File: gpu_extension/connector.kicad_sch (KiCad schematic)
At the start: 1 part

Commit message: schematic for gpu extension
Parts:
- J501: renamed from J; footprint (none) -> Connector_PinHeader_2.54mm:PinHeader_2x08_P2.54mm_Horizontal

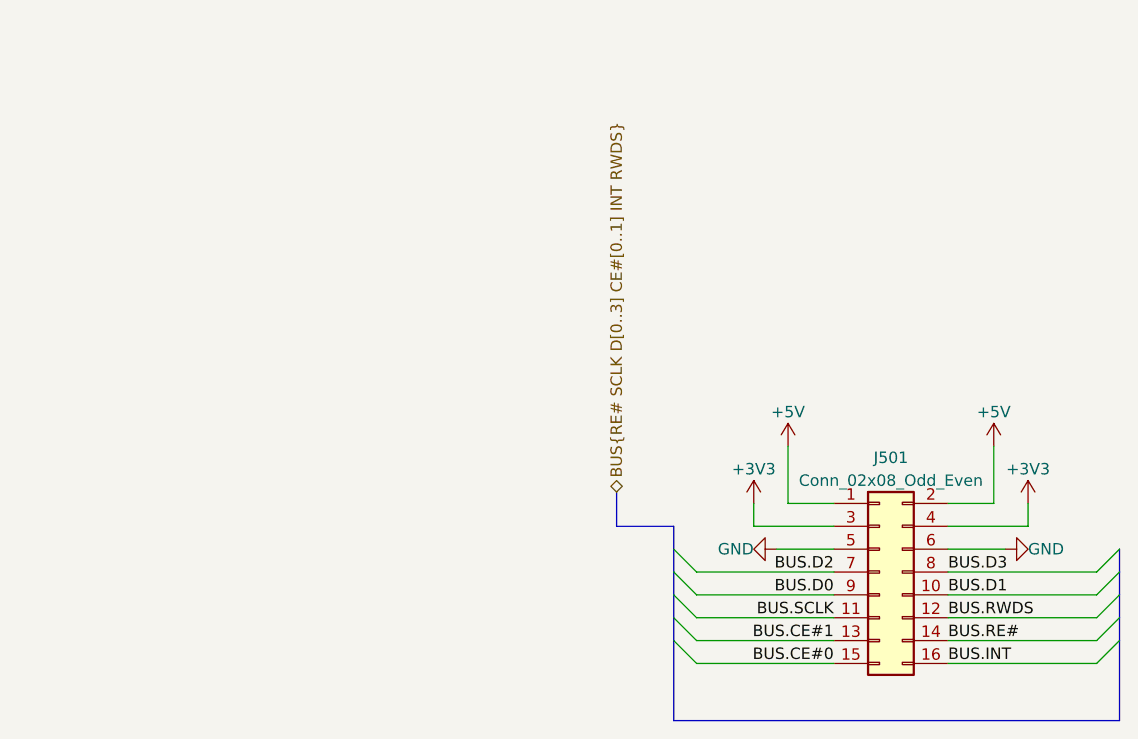
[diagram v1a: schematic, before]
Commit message: some ERC fixes
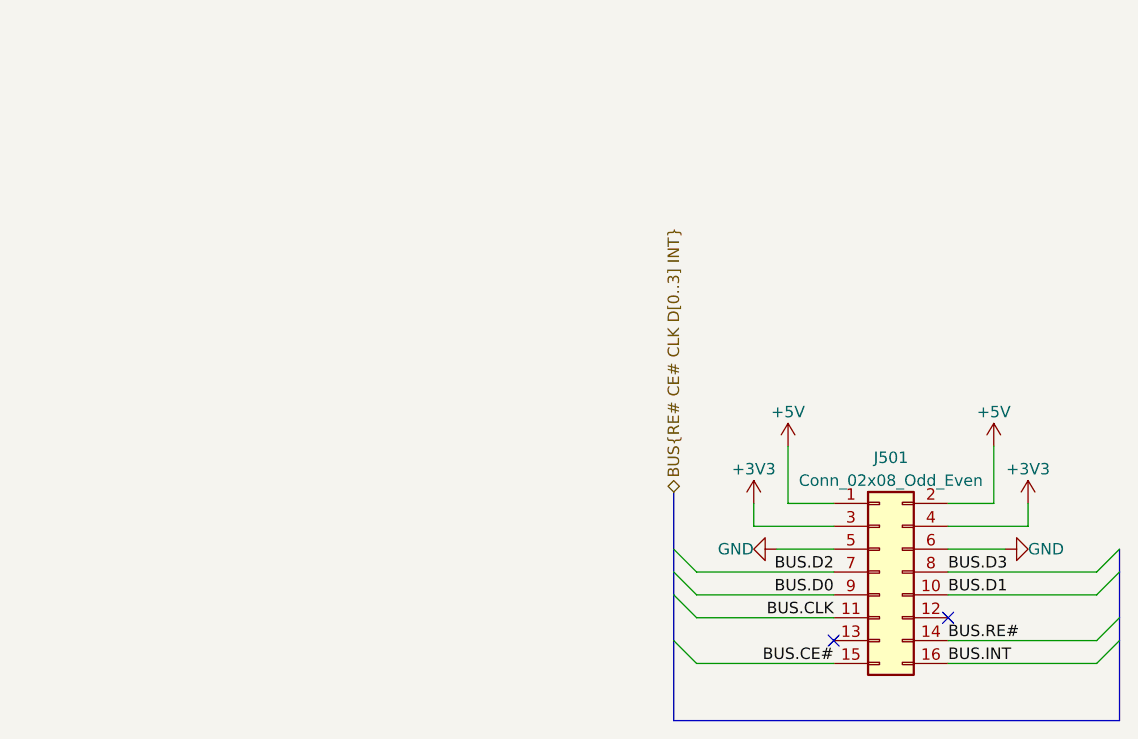
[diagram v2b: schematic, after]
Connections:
- net BUS.CE#0 renamed BUS.CE#
- net BUS.CE#1: no longer names the net of J501.13 (Pin_13)
- net BUS.RWDS: no longer names the net of J501.12 (Pin_12)
- net BUS.SCLK renamed BUS.CLK
- no-connect marks 0 -> 2
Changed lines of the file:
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@@
 (kicad_sch (version 20221004) (generator eeschema)
   (paper "A4")
+  (no_connect (at 115.57 83.82))
+  (no_connect (at 102.87 86.36))
   (bus_entry (at 132.08 86.36) (size 2.54 -2.54)
     (stroke (width 0) (type default))
@@
     (stroke (width 0) (type default))
   )
-  (bus_entry (at 132.08 78.74) (size 2.54 -2.54)
+  (bus_entry (at 87.63 83.82) (size -2.54 -2.54)
     (stroke (width 0) (type default))
   )
-  (bus_entry (at 87.63 86.36) (size -2.54 -2.54)
-    (stroke (width 0) (type default))
-  )
-  (bus_entry (at 132.08 83.82) (size 2.54 -2.54)
+  (bus_entry (at 132.08 78.74) (size 2.54 -2.54)
     (stroke (width 0) (type default))
   )
@@
     (stroke (width 0) (type default))
   )
-  (bus_entry (at 87.63 83.82) (size -2.54 -2.54)
-    (stroke (width 0) (type default))
-  )
   (bus_entry (at 132.08 88.9) (size 2.54 -2.54)
     (stroke (width 0) (type default))
   )
-  (bus (pts (xy 85.09 86.36) (xy 85.09 83.82))
+  (bus (pts (xy 85.09 78.74) (xy 85.09 81.28))
     (stroke (width 0) (type default))
   )
@@
     (stroke (width 0) (type default))
   )
-  (bus (pts (xy 85.09 81.28) (xy 85.09 78.74))
-    (stroke (width 0) (type default))
-  )
   (wire (pts (xy 120.65 71.12) (xy 115.57 71.12))
     (stroke (width 0) (type default))
   )
-  (bus (pts (xy 134.62 78.74) (xy 134.62 81.28))
-    (stroke (width 0) (type default))
-  )
-  (bus (pts (xy 85.09 83.82) (xy 85.09 81.28))
+  (bus (pts (xy 134.62 78.74) (xy 134.62 83.82))
     (stroke (width 0) (type default))
   )
@@
   )
   (wire (pts (xy 87.63 88.9) (xy 102.87 88.9))
-    (stroke (width 0) (type default))
-  )
-  (bus (pts (xy 85.09 73.66) (xy 78.74 73.66))
-    (stroke (width 0) (type default))
-  )
-  (bus (pts (xy 134.62 81.28) (xy 134.62 83.82))
     (stroke (width 0) (type default))
   )
@@
     (stroke (width 0) (type default))
   )
-  (bus (pts (xy 85.09 76.2) (xy 85.09 73.66))
+  (bus (pts (xy 134.62 95.25) (xy 85.09 95.25))
     (stroke (width 0) (type default))
   )
-  (bus (pts (xy 134.62 95.25) (xy 85.09 95.25))
+  (bus (pts (xy 85.09 81.28) (xy 85.09 86.36))
     (stroke (width 0) (type default))
   )
@@
     (stroke (width 0) (type default))
   )
-  (wire (pts (xy 115.57 83.82) (xy 132.08 83.82))
-    (stroke (width 0) (type default))
-  )
-  (bus (pts (xy 78.74 73.66) (xy 78.74 69.85))
+  (bus (pts (xy 85.09 69.85) (xy 85.09 76.2))
     (stroke (width 0) (type default))
   )
@@
     (stroke (width 0) (type default))
   )
-  (wire (pts (xy 87.63 86.36) (xy 102.87 86.36))
-    (stroke (width 0) (type default))
-  )
   (bus (pts (xy 85.09 95.25) (xy 85.09 86.36))
     (stroke (width 0) (type default))
@@
     (effects (font (size 1.27 1.27)) (justify left bottom))
   )
-  (label "BUS.CE#0" (at 102.87 88.9 0) (fields_autoplaced)
+  (label "BUS.CLK" (at 102.87 83.82 180) (fields_autoplaced)
+    (effects (font (size 1.27 1.27)) (justify right bottom))
+  )
+  (label "BUS.CE#" (at 102.87 88.9 0) (fields_autoplaced)
     (effects (font (size 1.27 1.27)) (justify right bottom))
   )
@@
     (effects (font (size 1.27 1.27)) (justify left bottom))
   )
-  (label "BUS.RWDS" (at 115.57 83.82 0) (fields_autoplaced)
-    (effects (font (size 1.27 1.27)) (justify left bottom))
-  )
-  (label "BUS.SCLK" (at 102.87 83.82 0) (fields_autoplaced)
-    (effects (font (size 1.27 1.27)) (justify right bottom))
-  )
   (label "BUS.D0" (at 102.87 81.28 0) (fields_autoplaced)
     (effects (font (size 1.27 1.27)) (justify right bottom))
@@
     (effects (font (size 1.27 1.27)) (justify left bottom))
   )
-  (label "BUS.CE#1" (at 102.87 86.36 0) (fields_autoplaced)
+  (label "BUS.D2" (at 102.87 78.74 180) (fields_autoplaced)
     (effects (font (size 1.27 1.27)) (justify right bottom))
   )
-  (label "BUS.D2" (at 102.87 78.74 180)
-    (effects (font (size 1.27 1.27)) (justify right bottom))
-  )
-  (hierarchical_label "BUS{RE# SCLK D[0..3] CE#[0..1] INT RWDS}" (shape bidirectional) (at 78.74 69.85 90) (fields_autoplaced)
+  (hierarchical_label "BUS{RE# CE# CLK D[0..3] INT}" (shape bidirectional) (at 85.09 69.85 90) (fields_autoplaced)
     (effects (font (size 1.27 1.27)) (justify left))
   )

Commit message: gpu and motherboard passes tests, now time for fpga
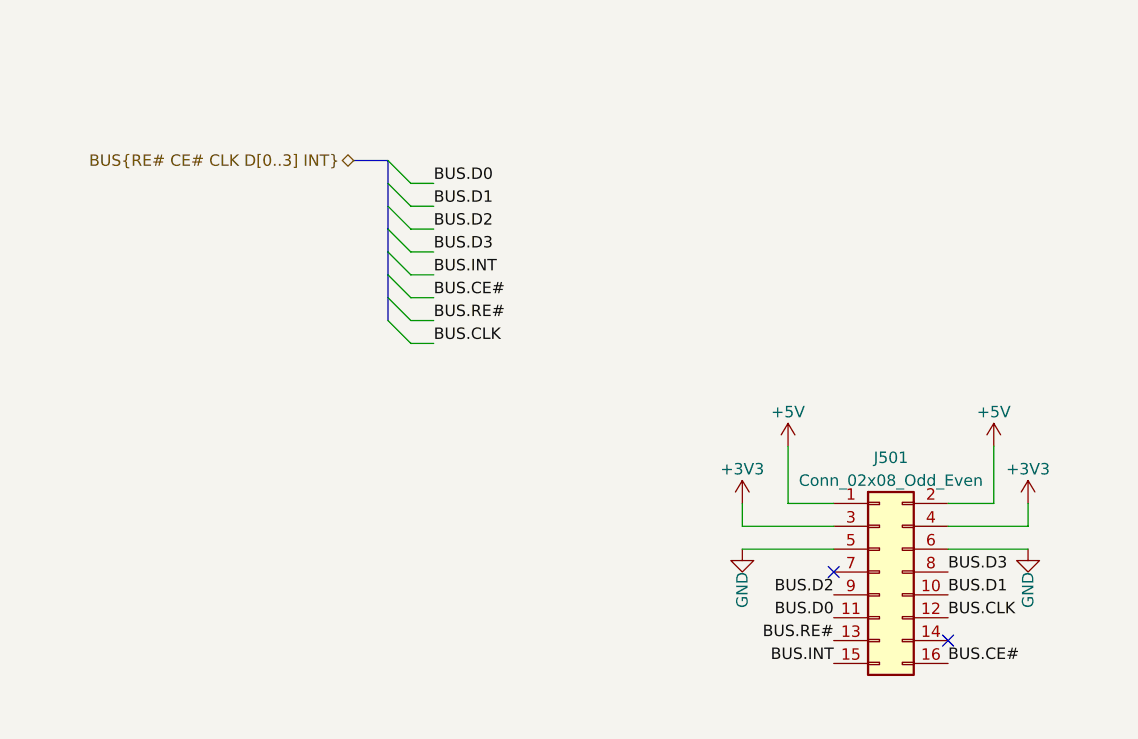
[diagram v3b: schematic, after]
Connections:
- net BUS.CE#: now also J501.16 (Pin_16); no longer J501.15 (Pin_15)
- net BUS.CLK: now also J501.12 (Pin_12); no longer J501.11 (Pin_11)
- net BUS.D0: now also J501.11 (Pin_11); no longer J501.9 (Pin_9)
- net BUS.D2: now also J501.9 (Pin_9); no longer J501.7 (Pin_7)
- net BUS.INT: now also J501.15 (Pin_15); no longer J501.16 (Pin_16)
- net BUS.RE#: now also J501.13 (Pin_13); no longer J501.14 (Pin_14)

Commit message: fixes in gpu extension schematic
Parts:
- removed J501: Conn_02x08_Odd_Even, Connector_PinHeader_2.54mm:PinHeader_2x08_P2.54mm_Horizontal, symbol Connector_Generic:Conn_02x08_Odd_Even
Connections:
- no-connect marks 2 -> 0
